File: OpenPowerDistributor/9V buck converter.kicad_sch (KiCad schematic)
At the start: 8 parts, among them U17 TPS565208DDA

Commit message: More schematic progress
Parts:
- removed C6: 10uF 50V, Capacitor_SMD:C_1206_3216Metric, symbol Device:C_Small
- removed C6: 47uF 16V, Capacitor_SMD:C_1210_3225Metric, symbol Device:C_Small
- removed L3: 3.3uH, Inductor_SMD:L_Bourns_SRP7028A_7.3x6.6mm, symbol Device:L_Small
- removed R167: 390k, Resistor_SMD:R_0603_1608Metric, symbol Device:R_Small
- removed R168: 49.9k, Resistor_SMD:R_0603_1608Metric, symbol Device:R_Small
- removed U17: TPS565208DDA, Package_SO:Texas_HSOP-8-1EP_3.9x4.9mm_P1.27mm, symbol Uli-RegSw:TPS565208DDA
- added C6: 47uF 16V, Capacitor_SMD:C_1210_3225Metric, symbol Device:C_Small
- added C6: 10uF 50V, Capacitor_SMD:C_1206_3216Metric, symbol Device:C_Small
- added L4: 3.3uH, Inductor_SMD:L_Bourns_SRP7028A_7.3x6.6mm, symbol Device:L_Small
- added R169: 390k, Resistor_SMD:R_0603_1608Metric, symbol Device:R_Small
- added R170: 49.9k, Resistor_SMD:R_0603_1608Metric, symbol Device:R_Small
- added U18: TPS565208DDA, Package_SO:Texas_HSOP-8-1EP_3.9x4.9mm_P1.27mm, symbol Uli-RegSw:TPS565208DDA
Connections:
- net +12V: now also U18.1 (EN), U18.8 (VIN)
- net GND: now also C6.1, C6.1, R170.2, U18.5 (GND), U18.9 (EP)
- net at C9.1: now also U18.7 (VBST)
- net at C9.2: now also L4.1, U18.6 (SW)
- net at C56.2: now also R169.2, R170.1, U18.2 (VFB)
- net +5V renamed +9V
- net +9V: now also C6.2, L4.2, R169.1
- new net: C6.2, U18.3 (VREG5)
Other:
- note added: "9.3V 5A buck converter"
- note removed: "5.3V 5A buck converter"

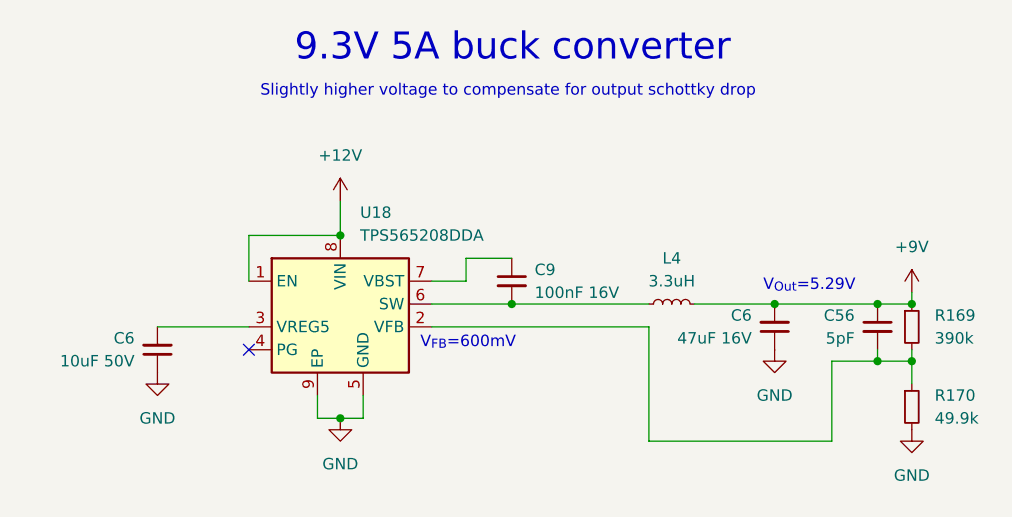
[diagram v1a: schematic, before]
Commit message: More work on schematic wiring
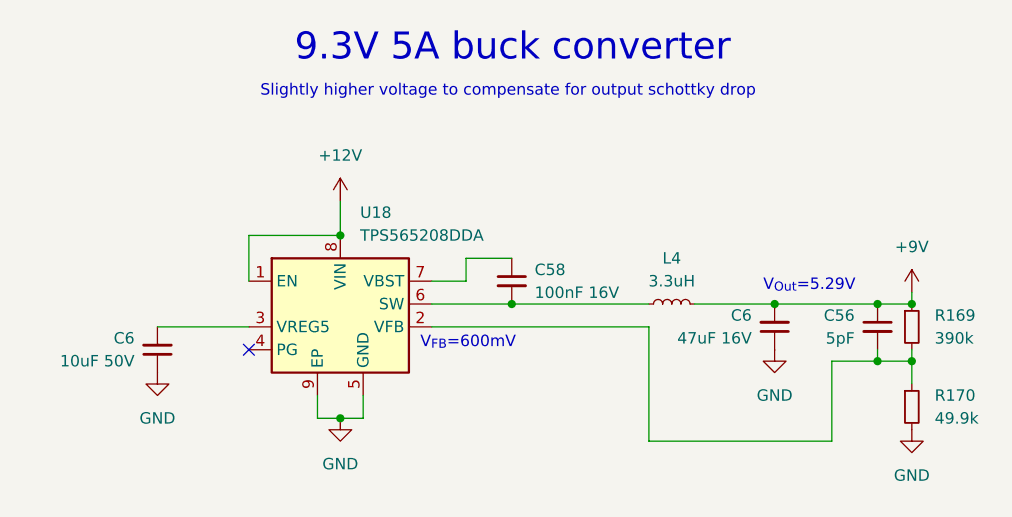
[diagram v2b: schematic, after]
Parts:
- renumbered C9 to C58
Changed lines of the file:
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@@
   (symbol (lib_id "Device:C_Small") (at 128.27 73.66 0) (unit 1)
     (in_bom yes) (on_board yes) (dnp no) (fields_autoplaced)
-    (property "Reference" "C9" (at 130.81 72.3963 0)
+    (property "Reference" "C58" (at 130.81 72.3963 0)
       (effects (font (size 1.27 1.27)) (justify left))
     )
@@
     (instances
       (project "OpenPowerDistribution"
-        (path "/df87b081-37a2-452c-8581-7eff2c408a17/b96d46bc-8ba1-4cbe-b99e-e39dc05b303c"
-          (reference "C9") (unit 1)
-        )
-        (path "/df87b081-37a2-452c-8581-7eff2c408a17/e4deee11-55f7-4f18-af99-bea885b0cfea"
-          (reference "C17") (unit 1)
-        )
-        (path "/df87b081-37a2-452c-8581-7eff2c408a17/85719244-66a7-40c3-82ed-28faeb6fb371"
-          (reference "C22") (unit 1)
-        )
-        (path "/df87b081-37a2-452c-8581-7eff2c408a17/74fd09d3-df1f-43b2-92e6-36c41e96448f"
-          (reference "C27") (unit 1)
-        )
-        (path "/df87b081-37a2-452c-8581-7eff2c408a17/e5191bda-9cfb-4a55-9ca3-cd9bac3e48c3"
-          (reference "C42") (unit 1)
-        )
-        (path "/df87b081-37a2-452c-8581-7eff2c408a17/c66097e8-d629-4b84-bed3-ecef8eda3008"
-          (reference "C37") (unit 1)
-        )
-        (path "/df87b081-37a2-452c-8581-7eff2c408a17/f02926a4-ecb0-4085-b2d0-fb1538d188c5"
-          (reference "C32") (unit 1)
-        )
-        (path "/df87b081-37a2-452c-8581-7eff2c408a17/3d9b216d-734e-4ffd-941d-a104869460a4"
-          (reference "C52") (unit 1)
-        )
-        (path "/df87b081-37a2-452c-8581-7eff2c408a17/f529eff0-84d8-4678-a1b3-b1f91f6d1c09"
-          (reference "C47") (unit 1)
-        )
         (path "/df87b081-37a2-452c-8581-7eff2c408a17/e80d9cb1-99ed-4151-affe-23d60cb9d8e2"
           (reference "C58") (unit 1)

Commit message: Start to make layout
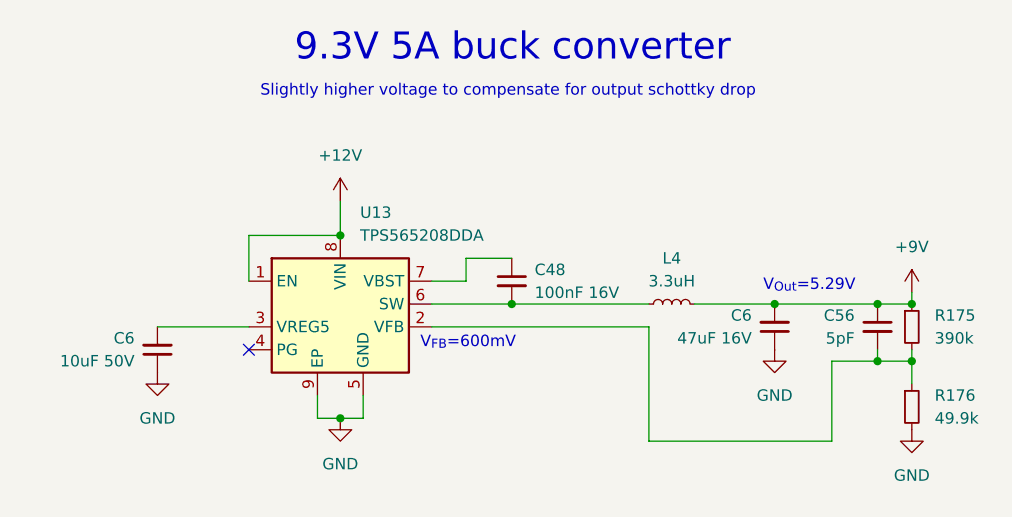
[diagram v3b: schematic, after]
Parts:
- renumbered C58 to C48, R169 to R175, R170 to R176, U18 to U13
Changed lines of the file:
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@@
   (symbol (lib_id "power:+9V") (at 172.72 74.93 0) (unit 1)
     (in_bom yes) (on_board yes) (dnp no) (fields_autoplaced)
-    (property "Reference" "#PWR0164" (at 172.72 78.74 0)
+    (property "Reference" "#PWR0169" (at 172.72 78.74 0)
       (effects (font (size 1.27 1.27)) hide)
     )
@@
       (project "OpenPowerDistribution"
         (path "/df87b081-37a2-452c-8581-7eff2c408a17/e80d9cb1-99ed-4151-affe-23d60cb9d8e2"
-          (reference "#PWR0164") (unit 1)
+          (reference "#PWR0169") (unit 1)
         )
       )
@@
   (symbol (lib_id "power:GND") (at 157.48 81.28 0) (unit 1)
     (in_bom yes) (on_board yes) (dnp no) (fields_autoplaced)
-    (property "Reference" "#PWR0163" (at 157.48 87.63 0)
+    (property "Reference" "#PWR0168" (at 157.48 87.63 0)
       (effects (font (size 1.27 1.27)) hide)
     )
@@
       (project "OpenPowerDistribution"
         (path "/df87b081-37a2-452c-8581-7eff2c408a17/e80d9cb1-99ed-4151-affe-23d60cb9d8e2"
-          (reference "#PWR0163") (unit 1)
+          (reference "#PWR0168") (unit 1)
         )
         (path "/df87b081-37a2-452c-8581-7eff2c408a17/c5ef4c26-c64f-4464-8506-0cba199ca76f"
@@
   (symbol (lib_id "power:+12V") (at 109.22 64.77 0) (unit 1)
     (in_bom yes) (on_board yes) (dnp no) (fields_autoplaced)
-    (property "Reference" "#PWR0161" (at 109.22 68.58 0)
+    (property "Reference" "#PWR0166" (at 109.22 68.58 0)
       (effects (font (size 1.27 1.27)) hide)
     )
@@
       (project "OpenPowerDistribution"
         (path "/df87b081-37a2-452c-8581-7eff2c408a17/e80d9cb1-99ed-4151-affe-23d60cb9d8e2"
-          (reference "#PWR0161") (unit 1)
+          (reference "#PWR0166") (unit 1)
         )
         (path "/df87b081-37a2-452c-8581-7eff2c408a17/c5ef4c26-c64f-4464-8506-0cba199ca76f"
@@
   (symbol (lib_id "Device:C_Small") (at 128.27 73.66 0) (unit 1)
     (in_bom yes) (on_board yes) (dnp no) (fields_autoplaced)
-    (property "Reference" "C58" (at 130.81 72.3963 0)
+    (property "Reference" "C48" (at 130.81 72.3963 0)
       (effects (font (size 1.27 1.27)) (justify left))
     )
@@
       (project "OpenPowerDistribution"
         (path "/df87b081-37a2-452c-8581-7eff2c408a17/e80d9cb1-99ed-4151-affe-23d60cb9d8e2"
-          (reference "C58") (unit 1)
+          (reference "C48") (unit 1)
         )
         (path "/df87b081-37a2-452c-8581-7eff2c408a17/c5ef4c26-c64f-4464-8506-0cba199ca76f"
@@
         )
         (path "/df87b081-37a2-452c-8581-7eff2c408a17/e80d9cb1-99ed-4151-affe-23d60cb9d8e2"
-          (reference "C59") (unit 1)
+          (reference "C49") (unit 1)
         )
         (path "/df87b081-37a2-452c-8581-7eff2c408a17/c5ef4c26-c64f-4464-8506-0cba199ca76f"
@@
         )
         (path "/df87b081-37a2-452c-8581-7eff2c408a17/e80d9cb1-99ed-4151-affe-23d60cb9d8e2"
-          (reference "C4") (unit 1)
+          (reference "C47") (unit 1)
         )
         (path "/df87b081-37a2-452c-8581-7eff2c408a17/c5ef4c26-c64f-4464-8506-0cba199ca76f"
@@
   (symbol (lib_id "Uli-RegSw:TPS565208DDA") (at 109.22 76.2 0) (unit 1)
     (in_bom yes) (on_board yes) (dnp no) (fields_autoplaced)
-    (property "Reference" "U18" (at 111.4141 66.04 0)
+    (property "Reference" "U13" (at 111.4141 66.04 0)
       (effects (font (size 1.27 1.27)) (justify left))
     )
@@
       (project "OpenPowerDistribution"
         (path "/df87b081-37a2-452c-8581-7eff2c408a17/e80d9cb1-99ed-4151-affe-23d60cb9d8e2"
-          (reference "U18") (unit 1)
+          (reference "U13") (unit 1)
         )
         (path "/df87b081-37a2-452c-8581-7eff2c408a17/c5ef4c26-c64f-4464-8506-0cba199ca76f"
@@
   (symbol (lib_id "power:GND") (at 172.72 90.17 0) (unit 1)
     (in_bom yes) (on_board yes) (dnp no) (fields_autoplaced)
-    (property "Reference" "#PWR0165" (at 172.72 96.52 0)
+    (property "Reference" "#PWR0170" (at 172.72 96.52 0)
       (effects (font (size 1.27 1.27)) hide)
     )
@@
       (project "OpenPowerDistribution"
         (path "/df87b081-37a2-452c-8581-7eff2c408a17/e80d9cb1-99ed-4151-affe-23d60cb9d8e2"
+          (reference "#PWR0170") (unit 1)
+        )
+        (path "/df87b081-37a2-452c-8581-7eff2c408a17/c5ef4c26-c64f-4464-8506-0cba199ca76f"
+          (reference "#PWR0159") (unit 1)
+        )
+      )
+    )
+  )
+  (symbol (lib_id "power:GND") (at 88.9 83.82 0) (unit 1)
+    (in_bom yes) (on_board yes) (dnp no) (fields_autoplaced)
+    (property "Reference" "#PWR0165" (at 88.9 90.17 0)
+      (effects (font (size 1.27 1.27)) hide)
+    )
+    (property "Value" "GND" (at 88.9 88.9 0)
+      (effects (font (size 1.27 1.27)))
+    )
+    (property "Footprint" "" (at 88.9 83.82 0)
+      (effects (font (size 1.27 1.27)) hide)
+    )
+    (property "Datasheet" "" (at 88.9 83.82 0)
+      (effects (font (size 1.27 1.27)) hide)
+    )
+    (pin "1")
+    (instances
+      (project "OpenPowerDistribution"
+        (path "/df87b081-37a2-452c-8581-7eff2c408a17/e80d9cb1-99ed-4151-affe-23d60cb9d8e2"
           (reference "#PWR0165") (unit 1)
         )
         (path "/df87b081-37a2-452c-8581-7eff2c408a17/c5ef4c26-c64f-4464-8506-0cba199ca76f"
-          (reference "#PWR0159") (unit 1)
-        )
-      )
-    )
-  )
-  (symbol (lib_id "power:GND") (at 88.9 83.82 0) (unit 1)
-    (in_bom yes) (on_board yes) (dnp no) (fields_autoplaced)
-    (property "Reference" "#PWR0160" (at 88.9 90.17 0)
-      (effects (font (size 1.27 1.27)) hide)
-    )
-    (property "Value" "GND" (at 88.9 88.9 0)
-      (effects (font (size 1.27 1.27)))
-    )
-    (property "Footprint" "" (at 88.9 83.82 0)
-      (effects (font (size 1.27 1.27)) hide)
-    )
-    (property "Datasheet" "" (at 88.9 83.82 0)
-      (effects (font (size 1.27 1.27)) hide)
-    )
-    (pin "1")
-    (instances
-      (project "OpenPowerDistribution"
-        (path "/df87b081-37a2-452c-8581-7eff2c408a17/e80d9cb1-99ed-4151-affe-23d60cb9d8e2"
-          (reference "#PWR0160") (unit 1)
-        )
-        (path "/df87b081-37a2-452c-8581-7eff2c408a17/c5ef4c26-c64f-4464-8506-0cba199ca76f"
           (reference "#PWR0154") (unit 1)
         )
@@
   (symbol (lib_id "power:GND") (at 109.22 88.9 0) (unit 1)
     (in_bom yes) (on_board yes) (dnp no) (fields_autoplaced)
-    (property "Reference" "#PWR0162" (at 109.22 95.25 0)
+    (property "Reference" "#PWR0167" (at 109.22 95.25 0)
       (effects (font (size 1.27 1.27)) hide)
     )
@@
       (project "OpenPowerDistribution"
         (path "/df87b081-37a2-452c-8581-7eff2c408a17/e80d9cb1-99ed-4151-affe-23d60cb9d8e2"
-          (reference "#PWR0162") (unit 1)
+          (reference "#PWR0167") (unit 1)
         )
         (path "/df87b081-37a2-452c-8581-7eff2c408a17/c5ef4c26-c64f-4464-8506-0cba199ca76f"
@@
   (symbol (lib_id "Device:R_Small") (at 172.72 87.63 0) (unit 1)
     (in_bom yes) (on_board yes) (dnp no) (fields_autoplaced)
-    (property "Reference" "R170" (at 175.26 86.36 0)
+    (property "Reference" "R176" (at 175.26 86.36 0)
       (effects (font (size 1.27 1.27)) (justify left))
     )
@@
       (project "OpenPowerDistribution"
         (path "/df87b081-37a2-452c-8581-7eff2c408a17/e80d9cb1-99ed-4151-affe-23d60cb9d8e2"
-          (reference "R170") (unit 1)
+          (reference "R176") (unit 1)
         )
         (path "/df87b081-37a2-452c-8581-7eff2c408a17/c5ef4c26-c64f-4464-8506-0cba199ca76f"
@@
   (symbol (lib_id "Device:R_Small") (at 172.72 78.74 0) (unit 1)
     (in_bom yes) (on_board yes) (dnp no) (fields_autoplaced)
-    (property "Reference" "R169" (at 175.26 77.47 0)
+    (property "Reference" "R175" (at 175.26 77.47 0)
       (effects (font (size 1.27 1.27)) (justify left))
     )
@@
       (project "OpenPowerDistribution"
         (path "/df87b081-37a2-452c-8581-7eff2c408a17/e80d9cb1-99ed-4151-affe-23d60cb9d8e2"
-          (reference "R169") (unit 1)
+          (reference "R175") (unit 1)
         )
         (path "/df87b081-37a2-452c-8581-7eff2c408a17/c5ef4c26-c64f-4464-8506-0cba199ca76f"
@@
         )
         (path "/df87b081-37a2-452c-8581-7eff2c408a17/e80d9cb1-99ed-4151-affe-23d60cb9d8e2"
-          (reference "C60") (unit 1)
-        )
-      )
+          (reference "C50") (unit 1)
+        )
+      )
